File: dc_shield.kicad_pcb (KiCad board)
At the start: 4 copper layers, 68.6 x 53.3 mm, 39 parts, among them J101 Vdrive, J102 Power, J103 Analog, J104 Digital/PWM, J105 Digital/PWM, J106 DC, J107 DC, Q101 SUD50P06-15, U101 VR10S12, U102 AT24C256C-SSHL-T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

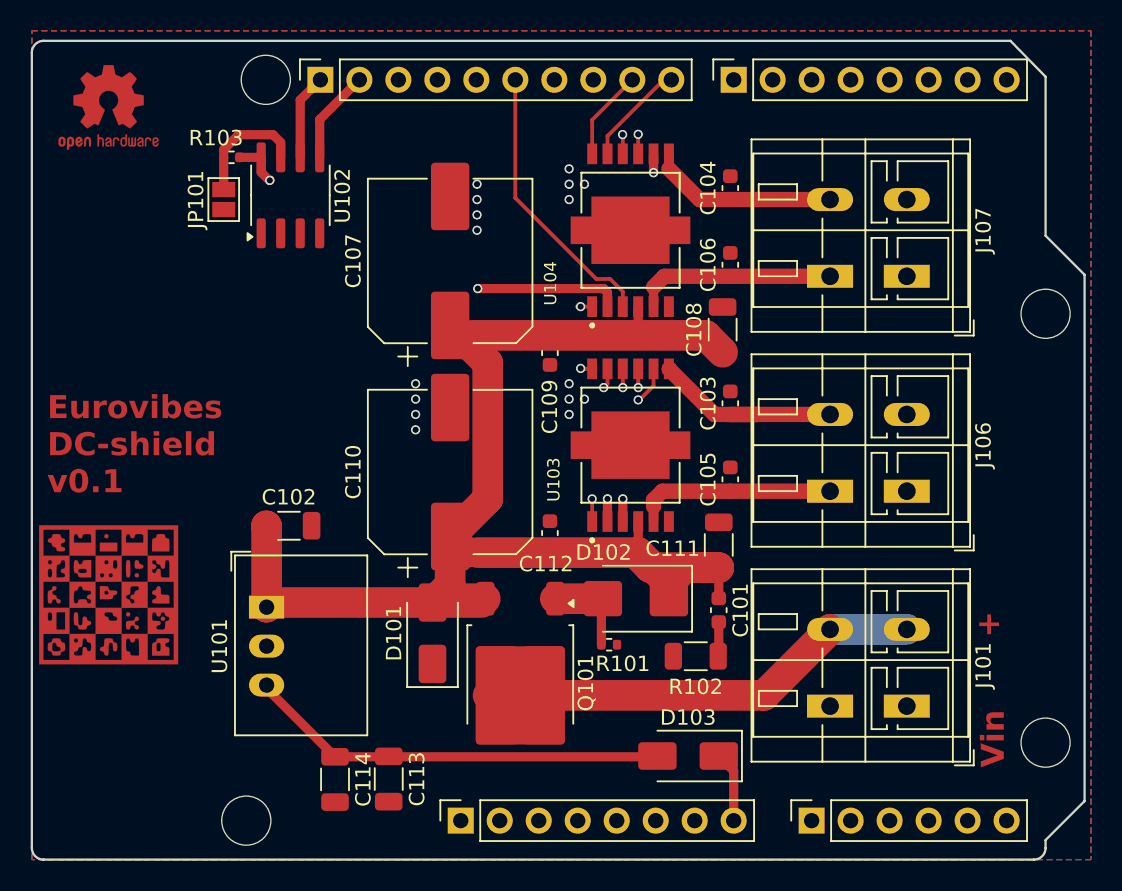
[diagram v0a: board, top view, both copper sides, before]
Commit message: Add current sensing
Signed-off-by: Benedikt Spranger <b.spranger@linutronix.de>
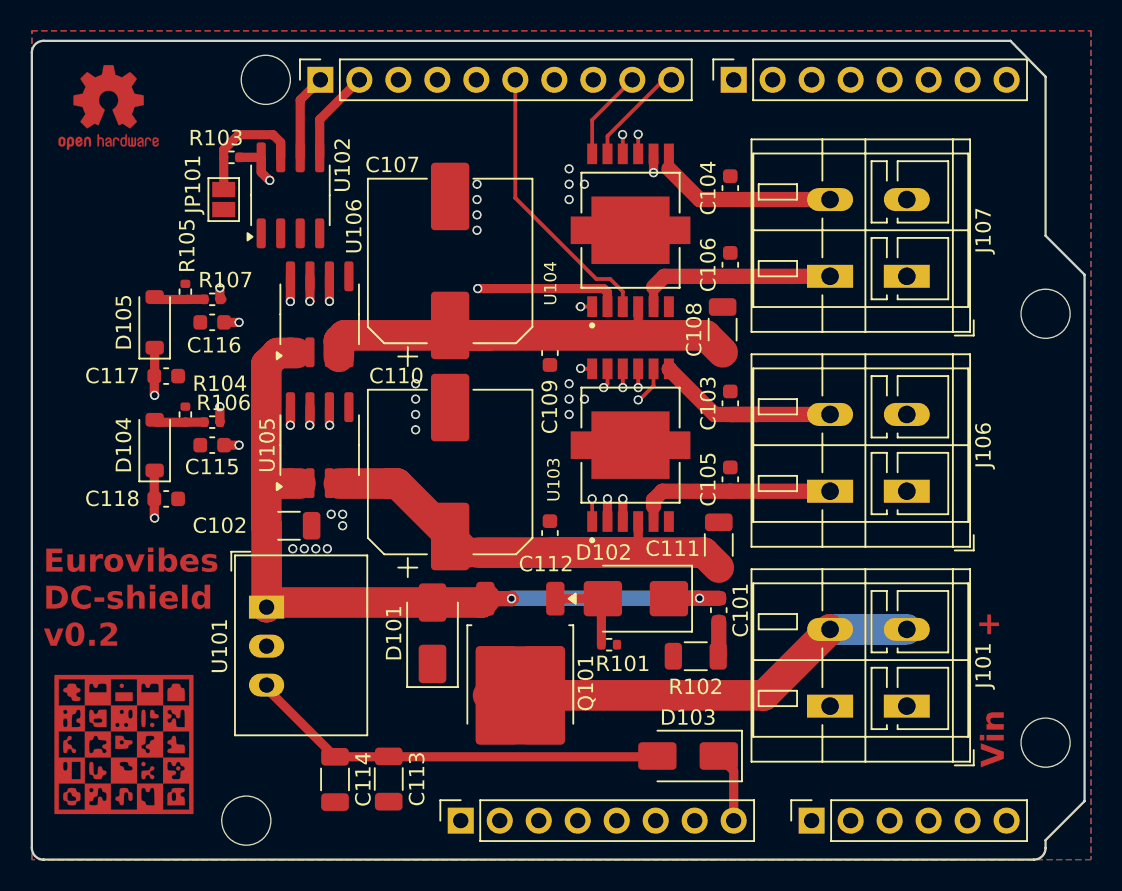
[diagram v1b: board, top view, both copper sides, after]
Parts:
- added C115: 1n, Capacitor_SMD:C_0603_1608Metric, F.Cu at (111.8, 73.0)
- added C116: 1n, Capacitor_SMD:C_0603_1608Metric, F.Cu at (111.8, 65.0)
- added C117: 100n, Capacitor_SMD:C_0603_1608Metric, F.Cu at (108.8, 68.5)
- added C118: 100n, Capacitor_SMD:C_0603_1608Metric, F.Cu at (108.8, 76.5)
- added D104: 1N4448W, Diode_SMD:D_SOD-123, F.Cu at (108.0, 73.0)
- added D105: 1N4448W, Diode_SMD:D_SOD-123, F.Cu at (108.0, 65.0)
- added R104: 10k, Resistor_SMD:R_0402_1005Metric, F.Cu at (110.0, 71.0)
- added R105: 10k, Resistor_SMD:R_0402_1005Metric, F.Cu at (110.0, 63.0)
- added R106: 2k, Resistor_SMD:R_0402_1005Metric, F.Cu at (111.8, 71.5)
- added R107: 2k, Resistor_SMD:R_0402_1005Metric, F.Cu at (111.8, 63.5)
- added U105: ACS712ELCTR-05B, Package_SO:SOIC-8_3.9x4.9mm_P1.27mm, F.Cu at (118.8, 73.0)
- added U106: ACS712ELCTR-05B, Package_SO:SOIC-8_3.9x4.9mm_P1.27mm, F.Cu at (118.8, 64.5)
- moved G*** 9.80 mm to (106.0, 92.5)
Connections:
- C107 pad 1: Vdrive -> /VdriveA
- C108 pad 1: Vdrive -> /VdriveA
- C109 pad 1: Vdrive -> /VdriveA
- C110 pad 1: Vdrive -> /VdriveB
- C111 pad 1: Vdrive -> /VdriveB
- C112 pad 1: Vdrive -> /VdriveB
- U103 pad 4: Vdrive -> /VdriveB
- U104 pad 4: Vdrive -> /VdriveA
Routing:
- net /A1: track 0.00 -> 70.5 mm, vias 0 -> 1
- net /A0: track 0.00 -> 58.6 mm, vias 0 -> 1
- net +5V: track 0.00 -> 45.4 mm, vias 0 -> 2
- net Vdrive: track 92.7 -> 52.0 mm, vias 0 -> 2
- net /VdriveB: track 0.00 -> 33.8 mm
- net /VdriveA: track 0.00 -> 29.8 mm
- net Net-(U106-FILTER): track 0.00 -> 9.06 mm, vias 0 -> 2
- net Net-(U106-VIOUT): track 0.00 -> 8.62 mm, vias 0 -> 2
- net Net-(U105-FILTER): track 0.00 -> 8.59 mm, vias 0 -> 2
- net Net-(U105-VIOUT): track 0.00 -> 8.53 mm, vias 0 -> 2
- net Net-(D104-A): track 0.00 -> 3.31 mm
- net Net-(D105-A): track 0.00 -> 3.31 mm
- net GND: vias 16 -> 23
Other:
- board text added: "Eurovibes DC-shield v0.2"
- board text removed: "Eurovibes DC-shield v0.1"

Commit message: Replace 5A current sensor by 20A variant
Signed-off-by: Benedikt Spranger <b.spranger@linutronix.de>
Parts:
- U105, U106: value ACS712ELCTR-05B -> ACS712ELCTR-20A

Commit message: Add filter capacitors
Signed-off-by: Benedikt Spranger <b.spranger@linutronix.de>
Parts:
- added C119: 100n, Capacitor_SMD:C_0603_1608Metric, F.Cu at (115.0, 62.8)
- added C120: 100n, Capacitor_SMD:C_0603_1608Metric, F.Cu at (137.2, 94.5)
- R102: value 1R1 -> 1
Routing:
- net +5V: track 45.4 -> 50.3 mm
